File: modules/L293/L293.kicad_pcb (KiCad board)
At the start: 2 copper layers, 40.6 x 40.6 mm, 24 parts, among them J1 2, J10 11, J11 12, J12 13, J13 A0, J14 A1, J15 A2, J16 A3, J17 A4, J18 A5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

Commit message: L293 sch
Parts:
- added C1: 0.1uF, Capacitor_SMD:C_0805_2012Metric_Pad1.15x1.40mm_HandSolder, B.Cu at (118.1, 86.4)
- added C2: 0.1uF, Capacitor_SMD:C_0805_2012Metric_Pad1.15x1.40mm_HandSolder, B.Cu at (104.1, 83.8)
- added J21: Pwr, TerminalBlock:TerminalBlock_bornier-2_P5.08mm, F.Cu at (106.7, 87.0)
- added J22: M1, TerminalBlock:TerminalBlock_bornier-2_P5.08mm, F.Cu at (100.3, 54.6)
- added J23: M2, TerminalBlock:TerminalBlock_bornier-2_P5.08mm, F.Cu at (113.0, 54.6)
- added U1: 74LVC1G79, Package_TO_SOT_SMD:SOT-23-5_HandSoldering, B.Cu at (118.1, 81.3)
- added U2: 74LVC1G79, Package_TO_SOT_SMD:SOT-23-5_HandSoldering, B.Cu at (118.1, 76.2)
- added U3: 74LVC1G79, Package_TO_SOT_SMD:SOT-23-5_HandSoldering, B.Cu at (118.1, 71.1)
- added U4: 74LVC1G79, Package_TO_SOT_SMD:SOT-23-5_HandSoldering, B.Cu at (118.1, 66.0)
- added U5: L293D, Package_DIP:DIP-16_W7.62mm, F.Cu at (101.6, 62.2)
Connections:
- J19 pad 1: Net-(J19-Pad1) -> VCC
- J20 pad 1: Net-(J20-Pad1) -> GND

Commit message: L293 pcb
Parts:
- C1: moved to F.Cu
- moved C1 15.1 mm to (116.1, 71.4)
- moved U1 2.69 mm to (116.2, 79.4)
- moved U2 2.69 mm to (116.2, 74.3)
- moved U3 2.69 mm to (116.2, 69.2)
- moved U4 2.69 mm to (116.2, 64.1)
- moved U5 1.42 mm to (100.3, 61.6)
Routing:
- net GND: track 0.00 -> 61.3 mm, vias 0 -> 4
- net VCC: track 0.00 -> 49.9 mm, vias 0 -> 4
- net Net-(J23-Pad1): track 0.00 -> 27.6 mm
- net Net-(J23-Pad2): track 0.00 -> 23.6 mm
- net Net-(J22-Pad2): track 0.00 -> 23.1 mm
- net Net-(J2-Pad1): track 0.00 -> 20.6 mm
- net Net-(U2-Pad4): track 0.00 -> 16.2 mm
- net Net-(J22-Pad1): track 0.00 -> 14.4 mm
- net Net-(C2-Pad2): track 0.00 -> 14.0 mm
- net Net-(J6-Pad1): track 0.00 -> 13.5 mm
- net Net-(U3-Pad4): track 0.00 -> 12.6 mm
- net Net-(J5-Pad1): track 0.00 -> 11.0 mm
- net Net-(J4-Pad1): track 0.00 -> 8.83 mm
- net Net-(J3-Pad1): track 0.00 -> 8.57 mm
- net Net-(U4-Pad4): track 0.00 -> 7.30 mm

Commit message: L293 pcb ready
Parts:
- added C3: 0.1uF, Capacitor_SMD:C_0805_2012Metric_Pad1.15x1.40mm_HandSolder, F.Cu at (110.5, 69.1)
- moved C2 5.62 mm to (98.7, 82.5)
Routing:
- net Net-(J10-Pad1): track 0.00 -> 42.9 mm
- net GND: track 61.3 -> 97.8 mm, vias 4 -> 5
- net Net-(U1-Pad4): track 0.00 -> 36.2 mm
- net Net-(J9-Pad1): track 0.00 -> 27.2 mm, vias 0 -> 1
- net Net-(J2-Pad1): track 20.6 -> 33.9 mm
- net VCC: track 49.9 -> 55.4 mm
- net Net-(C2-Pad2): track 14.0 -> 15.1 mm
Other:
- board text added: "Bat"
- board text added: "M1"
- board text added: "M2"

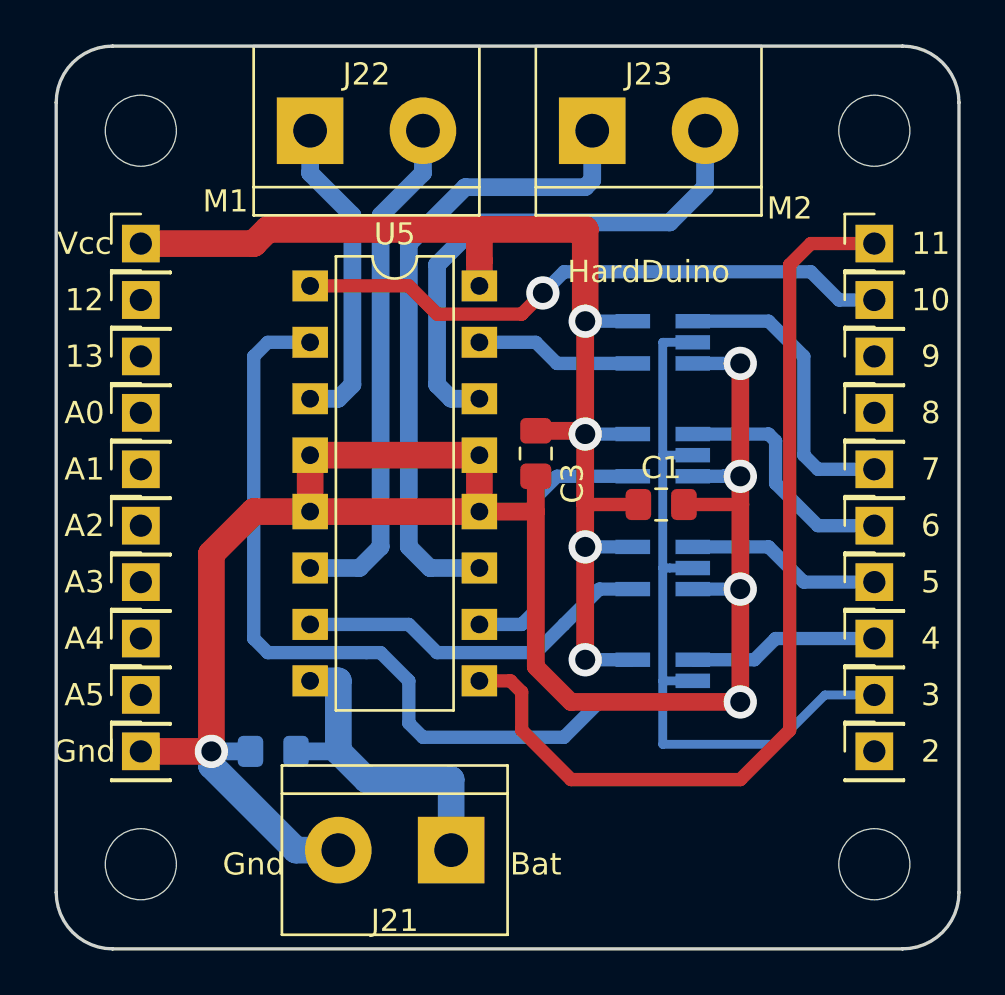
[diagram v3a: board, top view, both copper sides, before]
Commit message: Add pull-up and cap
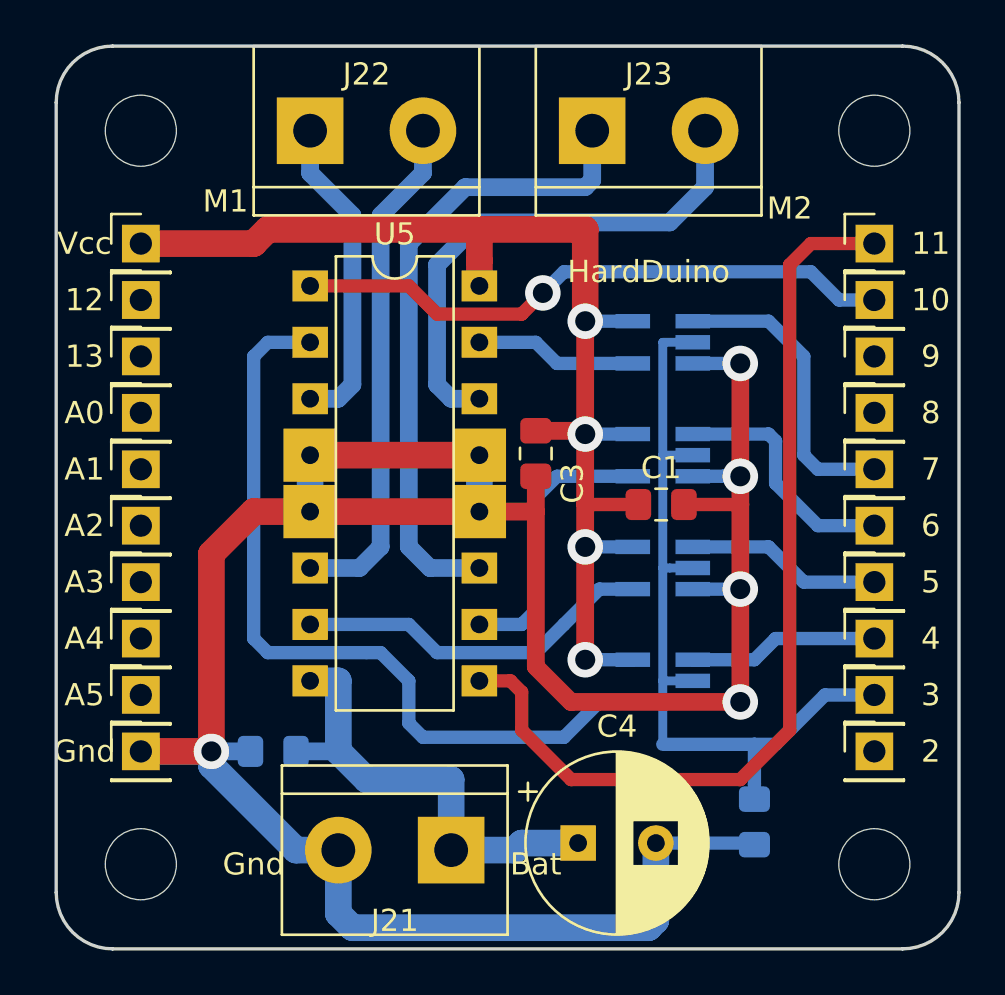
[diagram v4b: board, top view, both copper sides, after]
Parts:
- added C4: 500uF, Capacitor_THT:CP_Radial_D8.0mm_P3.50mm, F.Cu at (112.4, 86.7)
- added R1: 10k, Resistor_SMD:R_0805_2012Metric_Pad1.15x1.40mm_HandSolder, B.Cu at (120.3, 85.7)
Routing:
- net GND: track 97.8 -> 123.3 mm
- net Net-(C2-Pad2): track 15.1 -> 21.0 mm
- net Net-(J2-Pad1): track 33.9 -> 36.4 mm

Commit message: Add date. Add polygon.
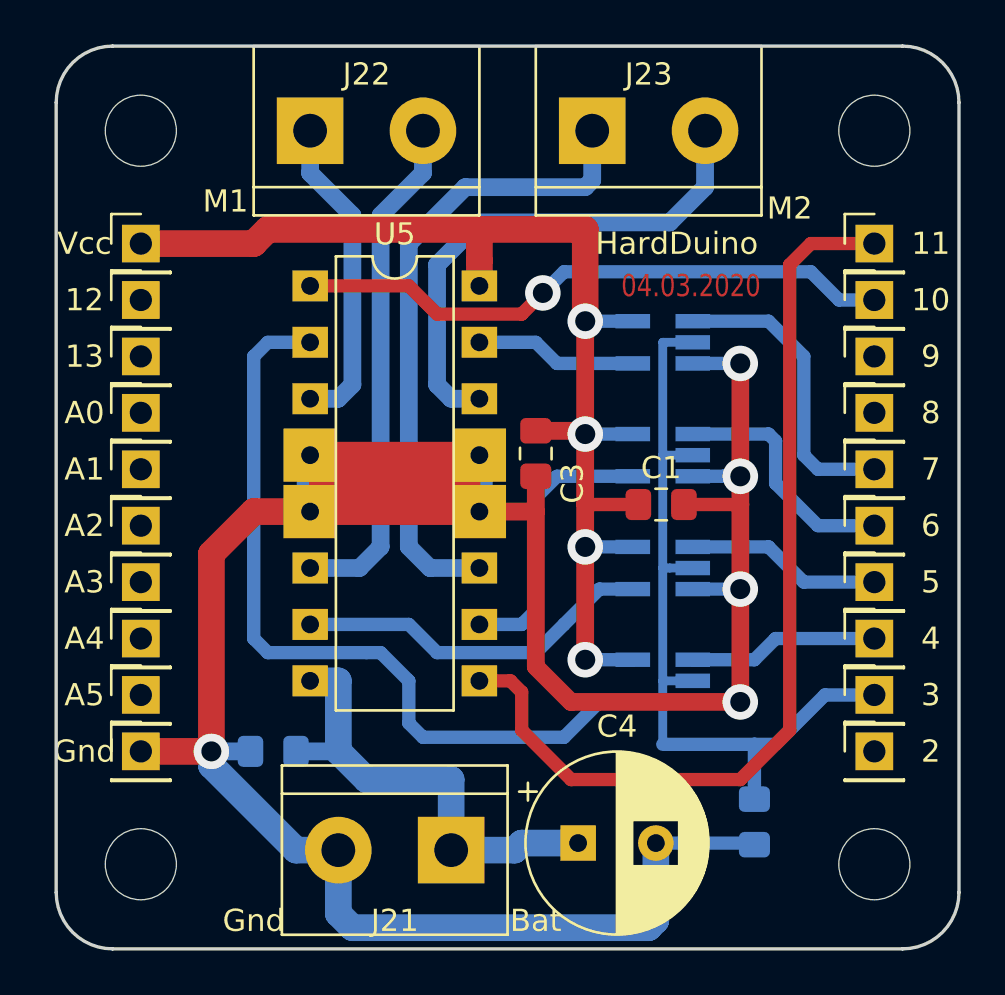
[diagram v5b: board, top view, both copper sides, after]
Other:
- board text added: "04.03.2020"
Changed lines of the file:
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@@
   (general
     (thickness 1.6)
-    (drawings 33)
+    (drawings 35)
     (tracks 185)
     (zones 0)
@@
   )
   (setup
-    (last_trace_width 1.2)
+    (last_trace_width 0.25)
     (user_trace_width 0.4)
     (user_trace_width 0.6)
@@
     )
   )
+  (gr_text 04.03.2020 (at 117.475 61.595) (layer F.Cu)
+    (effects (font (size 1 0.8) (thickness 0.15)))
+  )
+  (gr_poly (pts (xy 100.33 69.215) (xy 107.95 69.215) (xy 107.95 71.755) (xy 100.33 71.755)) (layer F.Cu) (width 0.1))
   (gr_text M2 (at 121.92 58.1025) (layer F.SilkS)
     (effects (font (size 1 1) (thickness 0.15)))
@@
     (effects (font (size 1 1) (thickness 0.15)))
   )
-  (gr_text Gnd (at 97.79 87.63) (layer F.SilkS)
+  (gr_text Gnd (at 97.79 90.17) (layer F.SilkS)
     (effects (font (size 1 1) (thickness 0.15)))
   )
-  (gr_text Bat (at 110.49 87.63) (layer F.SilkS)
+  (gr_text Bat (at 110.49 90.17) (layer F.SilkS)
     (effects (font (size 1 1) (thickness 0.15)))
   )
-  (gr_text HardDuino (at 115.57 60.96) (layer F.SilkS)
+  (gr_text HardDuino (at 116.84 59.69) (layer F.SilkS)
     (effects (font (size 1 1) (thickness 0.15)))
   )

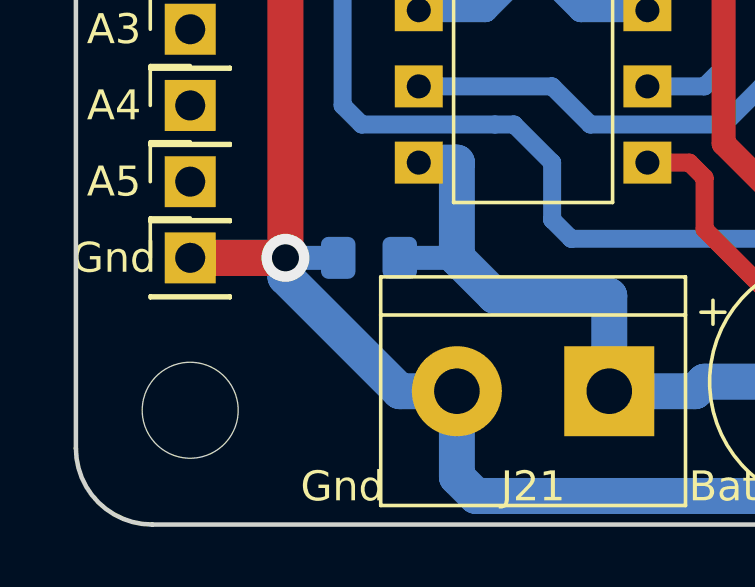
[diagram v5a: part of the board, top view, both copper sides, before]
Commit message: Add gnd symbol
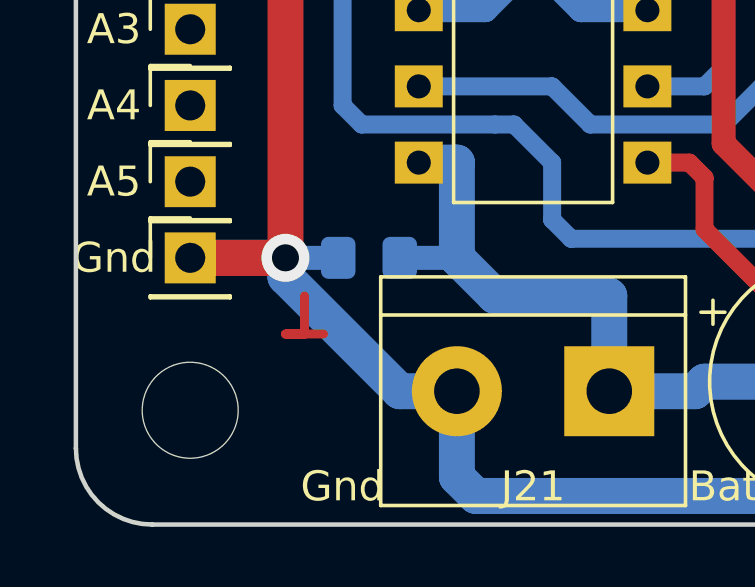
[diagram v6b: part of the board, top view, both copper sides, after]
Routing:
- net (no net): track 0.00 -> 3.17 mm
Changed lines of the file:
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@@
     (thickness 1.6)
     (drawings 35)
-    (tracks 185)
+    (tracks 188)
     (zones 0)
     (modules 37)
@@
   (gr_line (start 129.54 53.34) (end 129.54 88.9) (layer Edge.Cuts) (width 0.15))
   (gr_line (start 91.44 50.8) (end 127 50.8) (layer Edge.Cuts) (width 0.15))
+  (segment (start 96.52 83.82) (end 96.52 85.09) (width 0.3) (layer F.Cu) (net 0))
+  (segment (start 96.52 85.09) (end 95.885 85.09) (width 0.3) (layer F.Cu) (net 0))
+  (segment (start 95.885 85.09) (end 97.155 85.09) (width 0.3) (layer F.Cu) (net 0))
   (segment (start 116.205 69.215) (end 117.555 69.215) (width 0.4) (layer B.Cu) (net 2))
   (segment (start 117.555 64.135) (end 116.205 64.135) (width 0.4) (layer B.Cu) (net 2))
@@
   (segment (start 97.645 82.55) (end 95.885 82.55) (width 0.8) (layer B.Cu) (net 20))
   (segment (start 95.885 82.55) (end 95.885 82.55) (width 1.2) (layer B.Cu) (net 20))
-  (via (at 95.885 82.55) (size 1.6) (drill 0.9) (layers F.Cu B.Cu) (net 20) (status 1000000))
+  (via (at 95.885 82.55) (size 1.6) (drill 0.9) (layers F.Cu B.Cu) (net 20))
   (segment (start 110.49 70.1675) (end 110.49 71.755) (width 0.8) (layer F.Cu) (net 20))
   (segment (start 115.895 90.1625) (end 115.895 86.6775) (width 1.2) (layer B.Cu) (net 20))
